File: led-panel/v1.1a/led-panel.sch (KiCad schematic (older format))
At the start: 16 parts, among them J1 5V, J2 PMOD, J4 PMOD, J5 jmp, J6 Conn_02x08_Odd_Even, U1 SN74LVC8T245, U2 SN74LVC8T245

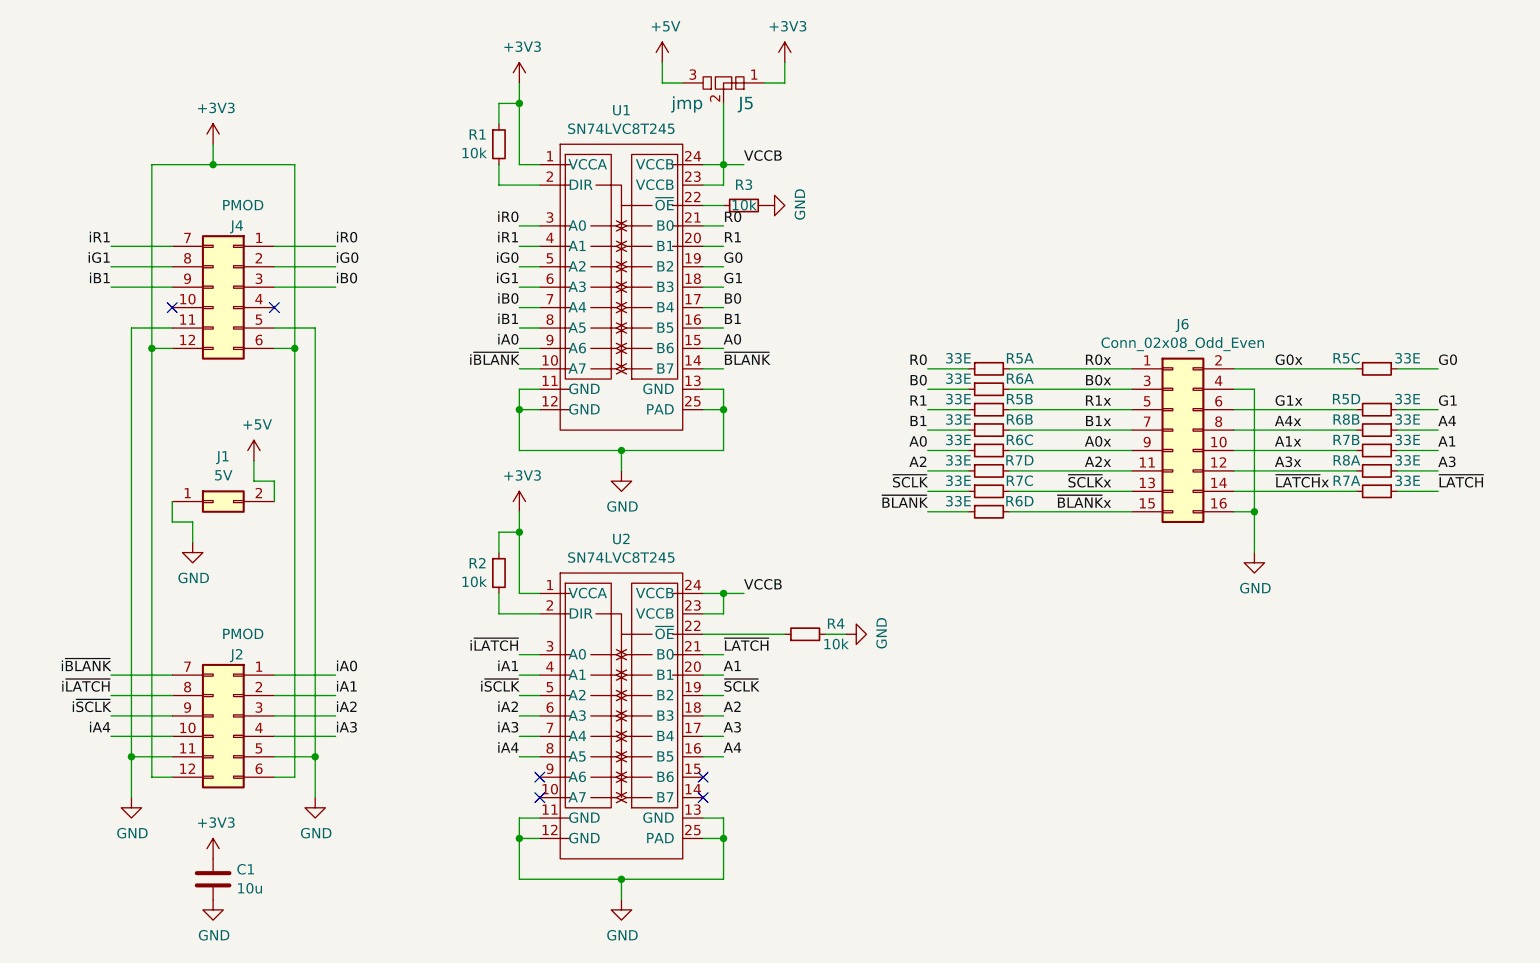
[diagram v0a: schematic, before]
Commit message: Corrected signal names for the LED panel PMOD.
The BLANK, LATCH, SCLK are all positive logic not negative.
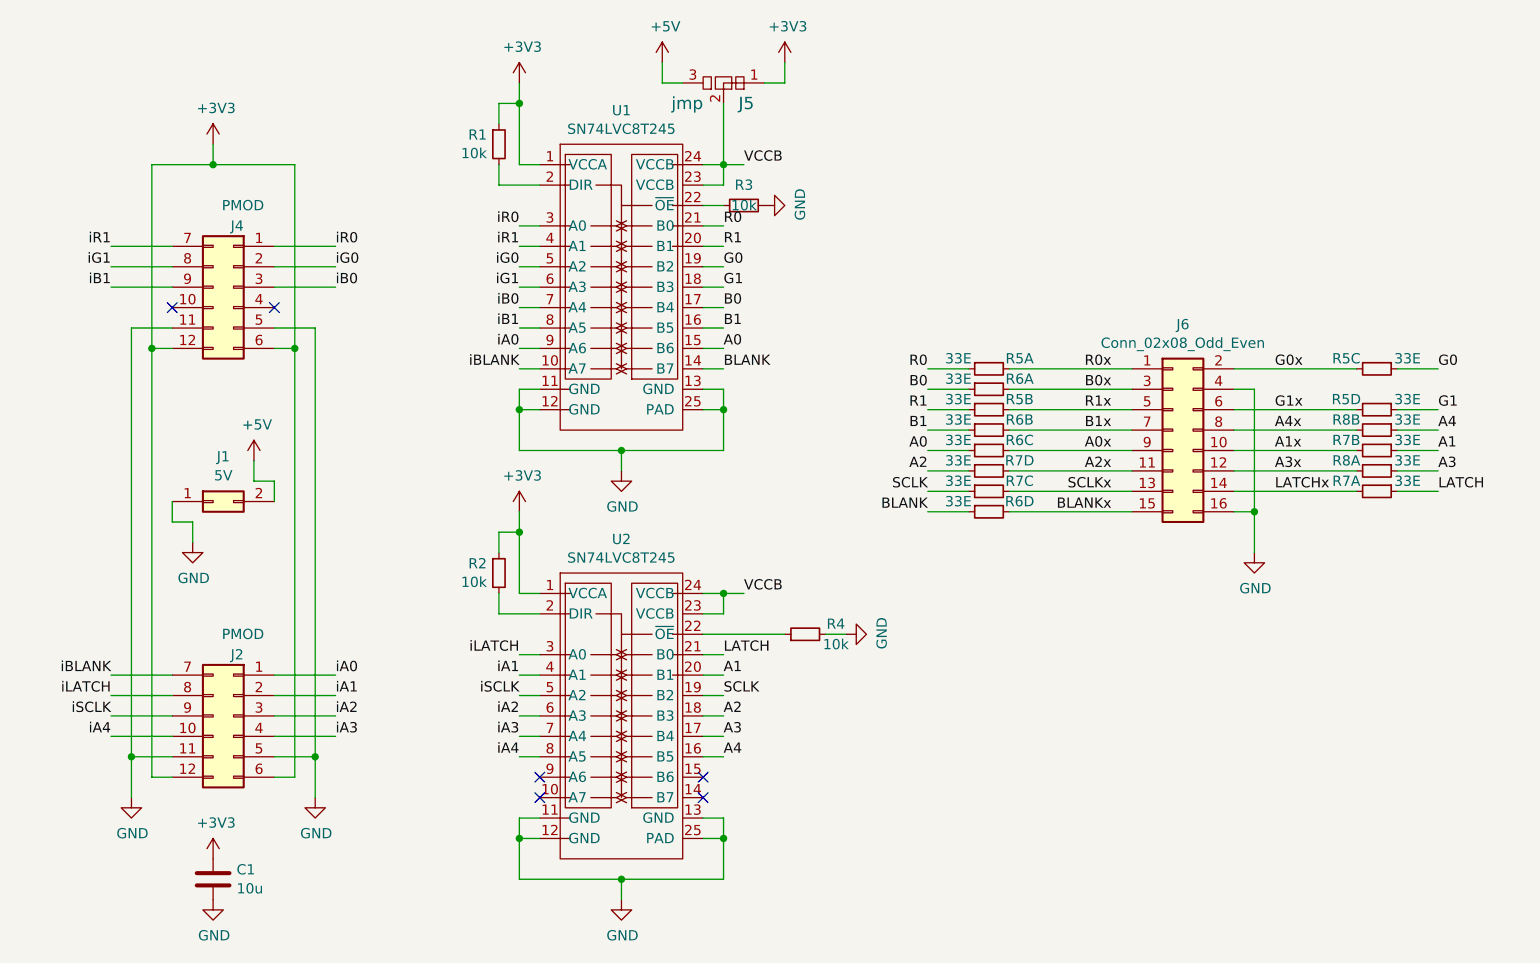
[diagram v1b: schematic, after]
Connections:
- net i~BLANK renamed iBLANK
- net i~LATCH renamed iLATCH
- net i~SCLK renamed iSCLK
- net ~BLANK renamed BLANK
- net ~BLANK~x renamed BLANKx
- net ~LATCH renamed LATCH
- net ~LATCH~x renamed LATCHx
- net ~SCLK renamed SCLK
- net ~SCLK~x renamed SCLKx
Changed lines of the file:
@@
 iA2
 Text Label 4100 4600 2    50   ~ 0
-i~SCLK
+iSCLK
 Text Label 5200 4500 0    50   ~ 0
 iA1
 Text Label 4100 4500 2    50   ~ 0
-i~LATCH
+iLATCH
 Text Label 5200 4400 0    50   ~ 0
 iA0
 Text Label 4100 4400 2    50   ~ 0
-i~BLANK
+iBLANK
 Text Label 5200 2500 0    50   ~ 0
 iB0
@@
 A3x
 Text Label 9000 3500 2    50   ~ 0
-~SCLK~x
+SCLKx
 Text Label 9800 3500 0    50   ~ 0
-~LATCH~x
+LATCHx
 Text Label 9000 3600 2    50   ~ 0
-~BLANK~x
+BLANKx
 $Comp
 L power:+3V3 #PWR0102
@@
 iA0
 Text Label 6100 2900 2    50   ~ 0
-i~BLANK
+iBLANK
 Text Label 7100 2200 0    50   ~ 0
 R0
@@
 A0
 Text Label 7100 2900 0    50   ~ 0
-~BLANK
+BLANK
 Wire Wire Line
 	7100 1900 7200 1900
@@
 	7000 4700 7100 4700
 Text Label 6100 4300 2    50   ~ 0
-i~LATCH
+iLATCH
 Text Label 6100 4400 2    50   ~ 0
 iA1
 Text Label 6100 4500 2    50   ~ 0
-i~SCLK
+iSCLK
 Text Label 6100 4600 2    50   ~ 0
 iA2
@@
 iA3
 Text Label 7100 4300 0    50   ~ 0
-~LATCH
+LATCH
 Text Label 7100 4400 0    50   ~ 0
 A1
 Text Label 7100 4500 0    50   ~ 0
-~SCLK
+SCLK
 Text Label 7100 4600 0    50   ~ 0
 A2
@@
 A2
 Text Label 8100 3500 2    50   ~ 0
-~SCLK
+SCLK
 Text Label 8100 3600 2    50   ~ 0
-~BLANK
+BLANK
 Wire Wire Line
 	8300 3100 8100 3100
@@
 A3
 Text Label 10600 3500 0    50   ~ 0
-~LATCH
+LATCH
 Wire Wire Line
 	10400 3200 10600 3200
